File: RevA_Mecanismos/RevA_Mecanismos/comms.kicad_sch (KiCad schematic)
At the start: 12 parts, among them IC1 MAX33040EAKA+T, J2 Conn_01x03_Pin, J3 430450224, J4 430450224, J6 430450224, J7 430450224

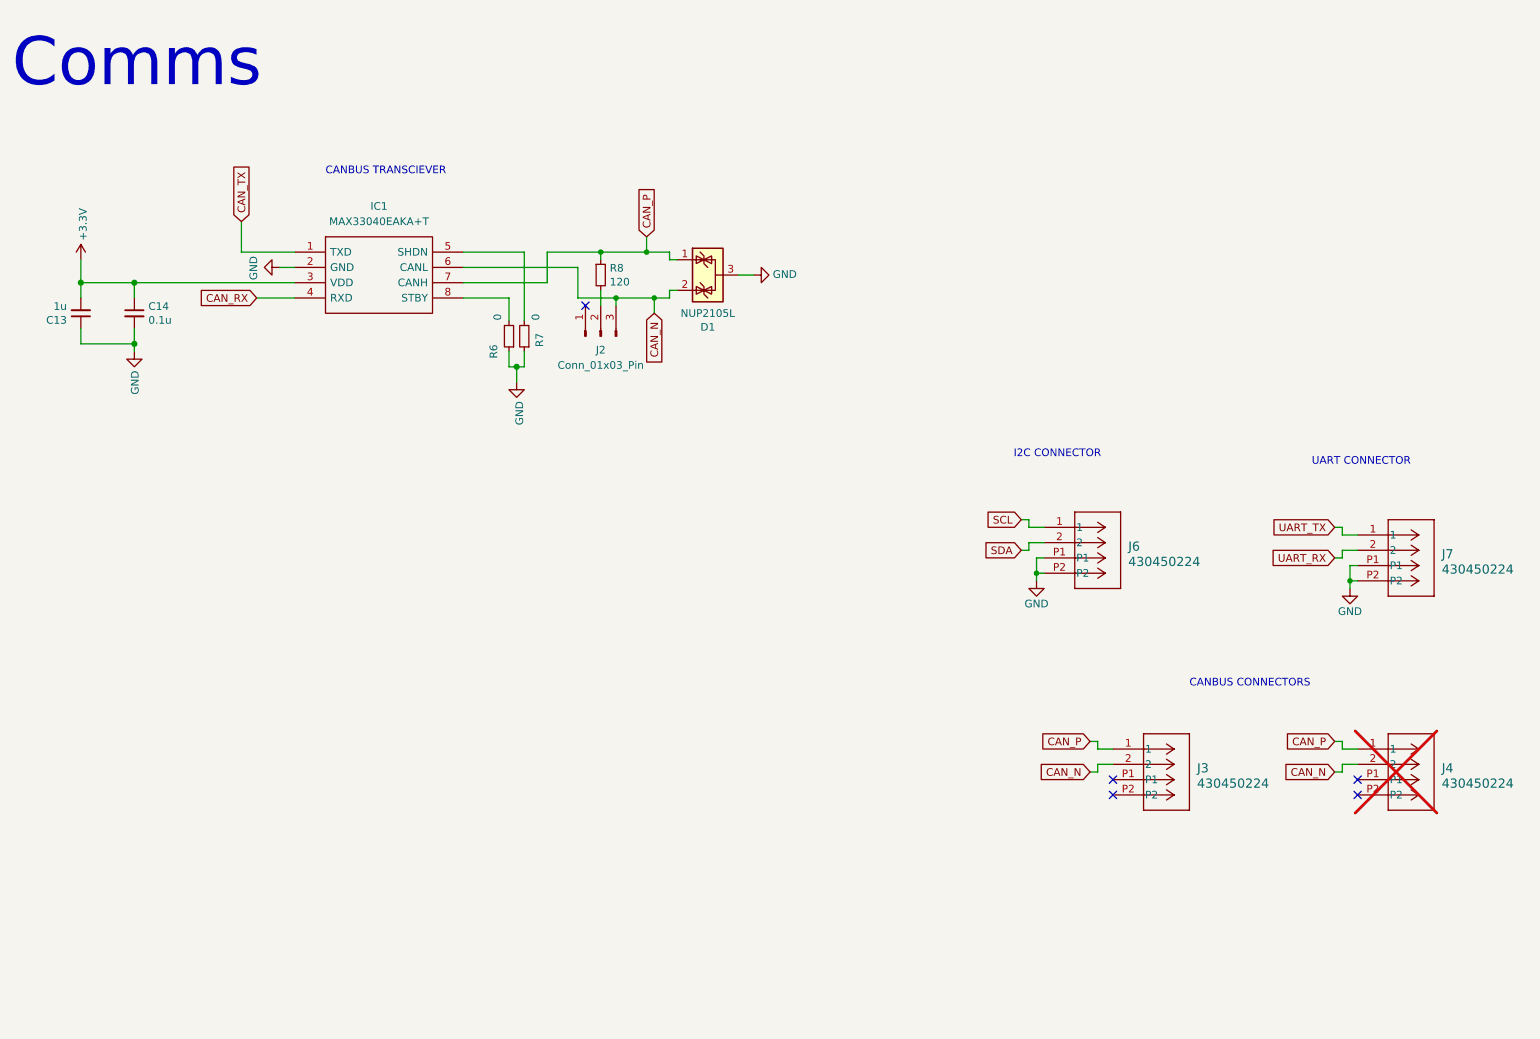
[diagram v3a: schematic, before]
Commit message: Updated STM32 USV Mechanism PCB
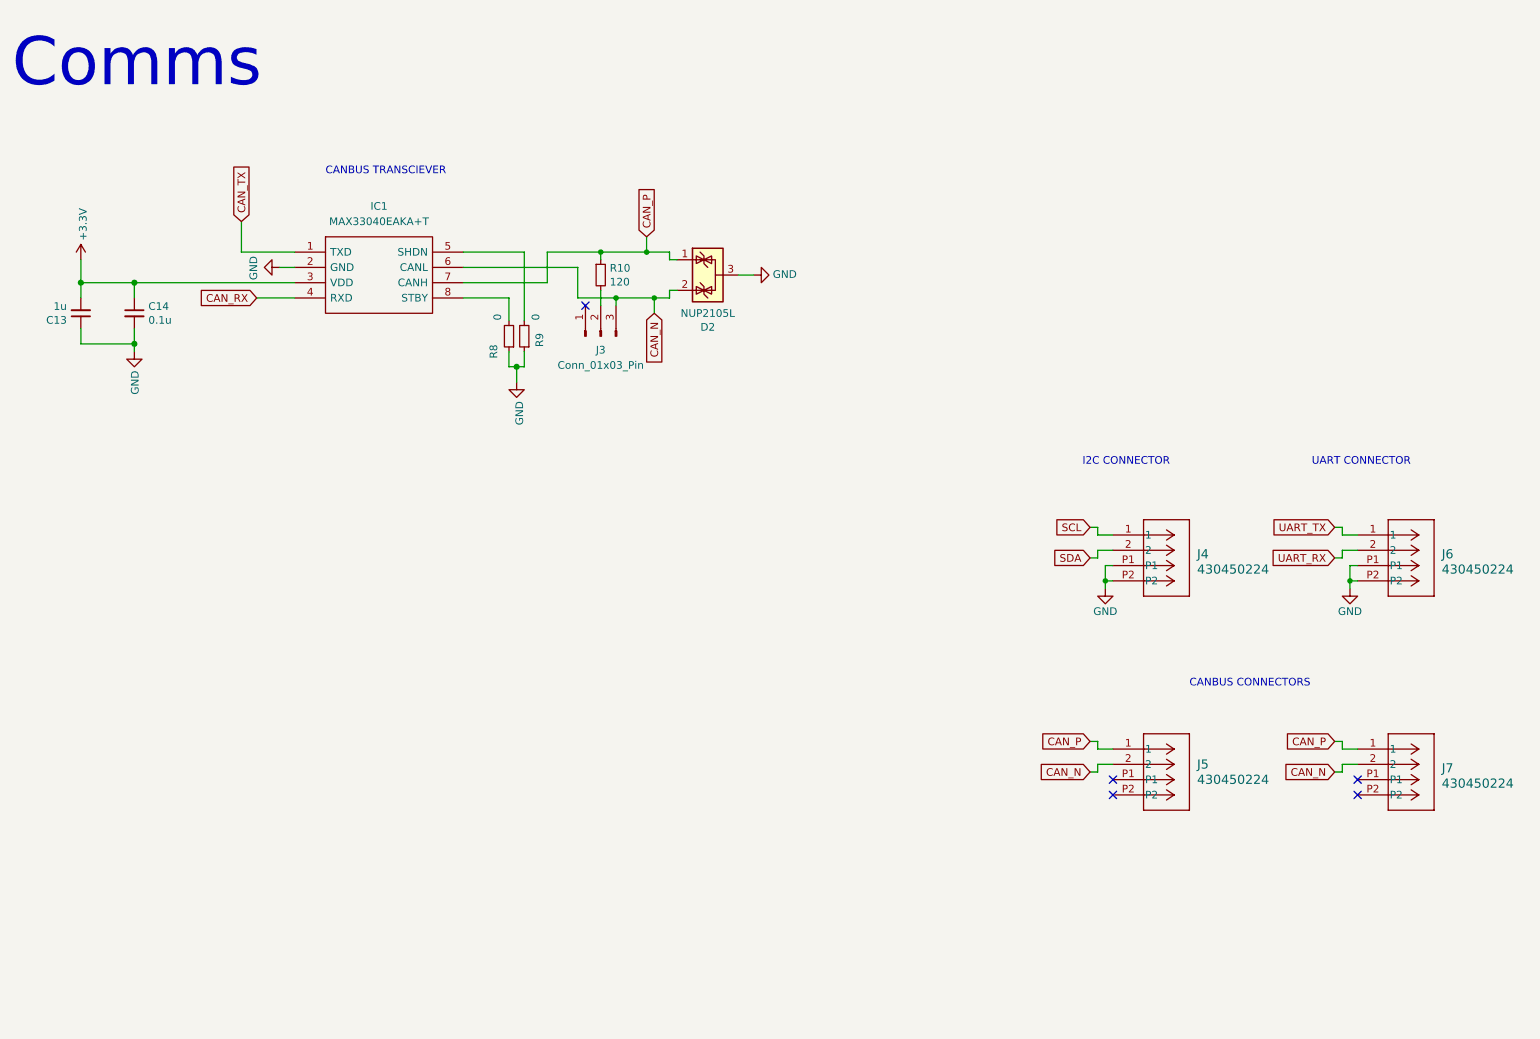
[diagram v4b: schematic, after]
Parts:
- J7: renamed from J4; now fitted
- renumbered D1 to D2, J2 to J3, J6 to J4, J3 to J5, J7 to J6, R8 to R10, R6 to R8, R7 to R9
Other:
- moved on the sheet: J4

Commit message: Complete schematic and pcb designs, routes missing and not yet complete
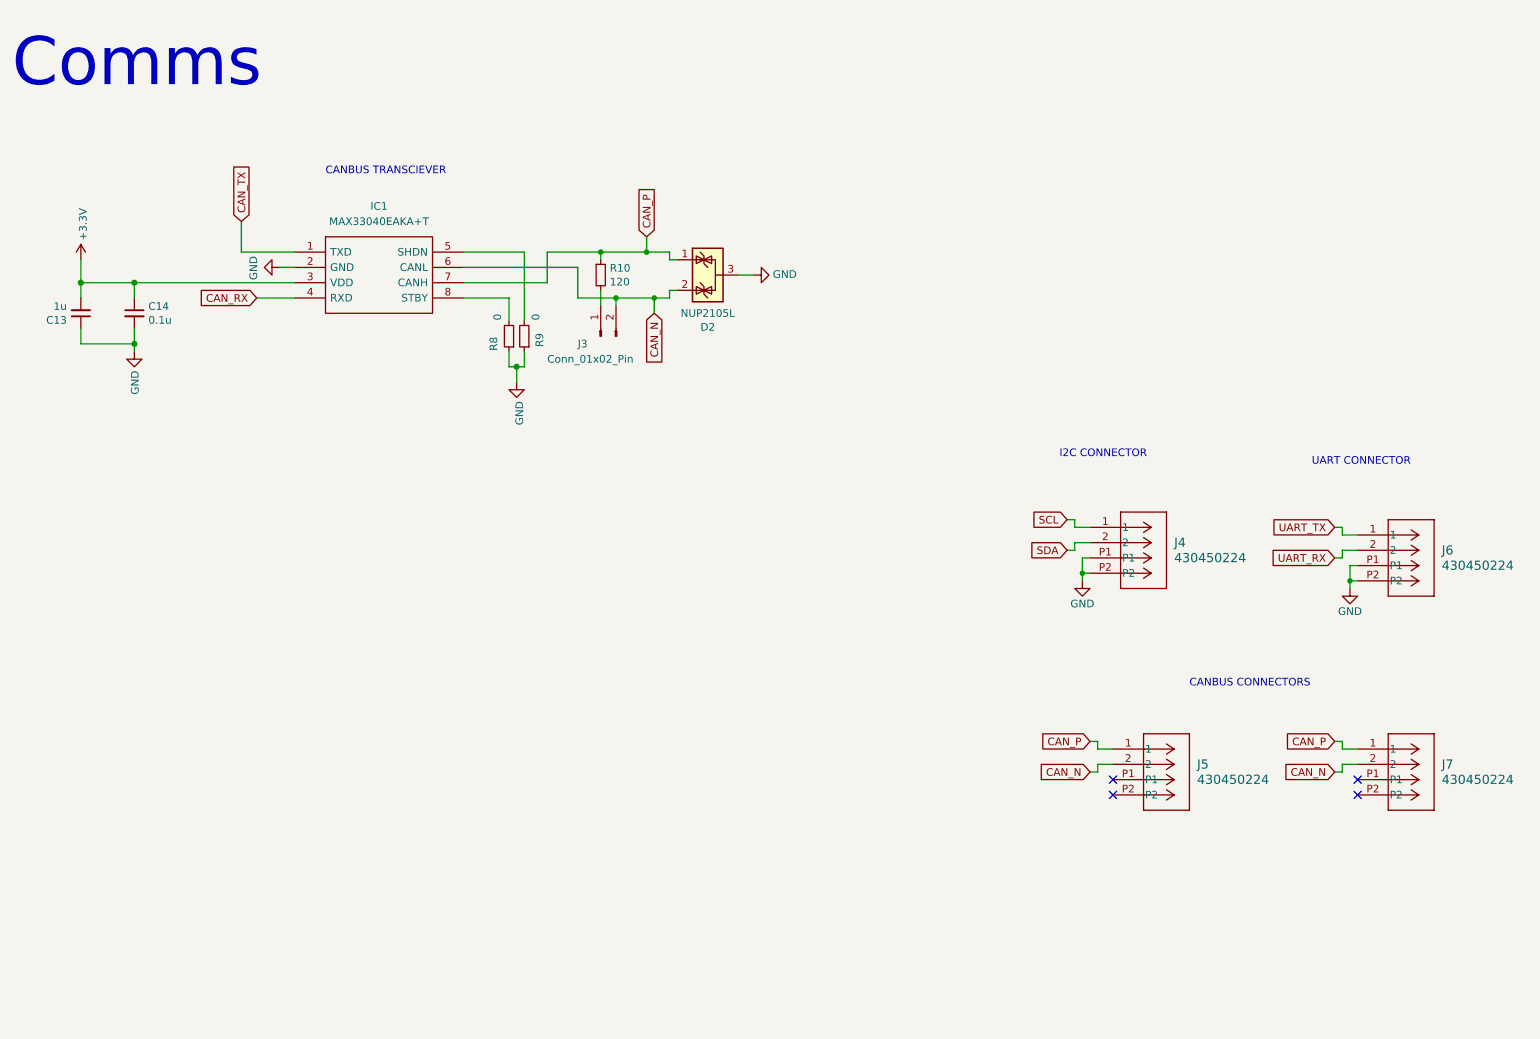
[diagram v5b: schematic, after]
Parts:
- removed J3: Conn_01x03_Pin, Connector_PinHeader_1.27mm:PinHeader_1x03_P1.27mm_Vertical, symbol Connector:Conn_01x03_Pin
- added J3: Conn_01x02_Pin, Connector_PinHeader_1.27mm:PinHeader_1x03_P1.27mm_Vertical, symbol Connector:Conn_01x02_Pin
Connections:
- net CAN_N: now also J3.2 (Pin_2)
- net at R10.2: now also J3.1 (Pin_1)
- no-connect marks 5 -> 4
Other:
- moved on the sheet: J4
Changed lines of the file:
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@@
   (junction (at 106.68 78.74) (diameter 1.016) (color 0 0 0 0)
   )
-  (junction (at 204.47 114.3) (diameter 0) (color 0 0 0 0)
+  (junction (at 200.66 113.03) (diameter 0) (color 0 0 0 0)
   )
   (junction (at 129.54 67.31) (diameter 0) (color 0 0 0 0)
@@
   (no_connect (at 246.38 147.32))
   (no_connect (at 205.74 149.86))
-  (no_connect (at 118.11 68.58))
   (wire (pts (xy 97.79 59.69) (xy 107.95 59.69))
     (stroke (width 0) (type default))
@@
     (stroke (width 0) (type solid))
   )
-  (wire (pts (xy 203.2 110.49) (xy 201.93 110.49))
+  (wire (pts (xy 199.39 109.22) (xy 198.12 109.22))
     (stroke (width 0) (type default))
   )
@@
     (stroke (width 0) (type solid))
   )
-  (wire (pts (xy 203.2 106.68) (xy 205.74 106.68))
-    (stroke (width 0) (type default))
-  )
-  (wire (pts (xy 204.47 115.57) (xy 204.47 114.3))
+  (wire (pts (xy 199.39 105.41) (xy 201.93 105.41))
+    (stroke (width 0) (type default))
+  )
+  (wire (pts (xy 200.66 114.3) (xy 200.66 113.03))
     (stroke (width 0) (type default))
   )
@@
     (stroke (width 0) (type default))
   )
-  (wire (pts (xy 203.2 110.49) (xy 203.2 109.22))
+  (wire (pts (xy 199.39 109.22) (xy 199.39 107.95))
     (stroke (width 0) (type default))
   )
@@
     (stroke (width 0) (type default))
   )
-  (wire (pts (xy 203.2 105.41) (xy 203.2 106.68))
+  (wire (pts (xy 199.39 104.14) (xy 199.39 105.41))
     (stroke (width 0) (type default))
   )
@@
     (stroke (width 0) (type solid))
   )
-  (wire (pts (xy 204.47 111.76) (xy 205.74 111.76))
-    (stroke (width 0) (type default))
-  )
-  (wire (pts (xy 204.47 114.3) (xy 204.47 111.76))
+  (wire (pts (xy 200.66 110.49) (xy 201.93 110.49))
+    (stroke (width 0) (type default))
+  )
+  (wire (pts (xy 200.66 113.03) (xy 200.66 110.49))
     (stroke (width 0) (type default))
   )
@@
     (stroke (width 0) (type default))
   )
-  (wire (pts (xy 203.2 109.22) (xy 205.74 109.22))
+  (wire (pts (xy 199.39 107.95) (xy 201.93 107.95))
     (stroke (width 0) (type default))
   )
@@
     (stroke (width 0) (type solid))
   )
-  (wire (pts (xy 201.93 105.41) (xy 203.2 105.41))
+  (wire (pts (xy 198.12 104.14) (xy 199.39 104.14))
     (stroke (width 0) (type default))
   )
@@
     (stroke (width 0) (type default))
   )
-  (wire (pts (xy 204.47 114.3) (xy 205.74 114.3))
+  (wire (pts (xy 200.66 113.03) (xy 201.93 113.03))
     (stroke (width 0) (type default))
   )
@@
     (effects (font (size 1.27 1.27)) (justify left bottom))
   )
-  (text "I2C CONNECTOR" (at 200.66 95.25 0)
+  (text "I2C CONNECTOR" (at 196.85 93.98 0)
     (effects (font (size 1.27 1.27)) (justify left bottom))
   )
@@
     )
   )
-  (global_label "SCL" (shape input) (at 201.93 105.41 180) (fields_autoplaced)
+  (global_label "SCL" (shape input) (at 198.12 104.14 180) (fields_autoplaced)
     (effects (font (size 1.27 1.27)) (justify right))
-    (property "Intersheetrefs" "${INTERSHEET_REFS}" (at 195.5166 105.41 0)
+    (property "Intersheetrefs" "${INTERSHEET_REFS}" (at 191.7066 104.14 0)
       (effects (font (size 1.27 1.27)) (justify right) hide)
     )
@@
     )
   )
-  (global_label "SDA" (shape input) (at 201.93 110.49 180) (fields_autoplaced)
+  (global_label "SDA" (shape input) (at 198.12 109.22 180) (fields_autoplaced)
     (effects (font (size 1.27 1.27)) (justify right))
-    (property "Intersheetrefs" "${INTERSHEET_REFS}" (at 195.4561 110.49 0)
+    (property "Intersheetrefs" "${INTERSHEET_REFS}" (at 191.6461 109.22 0)
       (effects (font (size 1.27 1.27)) (justify right) hide)
     )
@@
   (symbol (lib_id "Device:R_Small") (at 105.41 73.66 180) (unit 1)
     (in_bom yes) (on_board yes) (dnp no)
-    (property "Reference" "R8" (at 102.87 76.2 90)
+    (property "Reference" "R8" (at 102.87 74.93 90)
       (effects (font (size 1.27 1.27)))
     )
@@
     )
   )
-  (symbol (lib_id "power:GND") (at 204.47 115.57 0) (unit 1)
-    (in_bom yes) (on_board yes) (dnp no)
-    (property "Reference" "#PWR026" (at 204.47 121.92 0)
-      (effects (font (size 1.27 1.27)) hide)
-    )
-    (property "Value" "GND" (at 204.47 119.38 0)
+  (symbol (lib_id "power:GND") (at 200.66 114.3 0) (unit 1)
+    (in_bom yes) (on_board yes) (dnp no)
+    (property "Reference" "#PWR026" (at 200.66 120.65 0)
+      (effects (font (size 1.27 1.27)) hide)
+    )
+    (property "Value" "GND" (at 200.66 118.11 0)
       (effects (font (size 1.27 1.27)))
     )
-    (property "Footprint" "" (at 204.47 115.57 0)
-      (effects (font (size 1.27 1.27)) hide)
-    )
-    (property "Datasheet" "" (at 204.47 115.57 0)
+    (property "Footprint" "" (at 200.66 114.3 0)
+      (effects (font (size 1.27 1.27)) hide)
+    )
+    (property "Datasheet" "" (at 200.66 114.3 0)
       (effects (font (size 1.27 1.27)) hide)
     )
@@
   (symbol (lib_id "MolexConnectors:430450224") (at 246.38 106.68 0) (unit 1)
     (in_bom yes) (on_board yes) (dnp no) (fields_autoplaced)
-    (property "Reference" "J6" (at 260.35 109.855 0)
+    (property "Reference" "J6" (at 260.35 109.22 0)
       (effects (font (size 1.524 1.524)) (justify left))
     )
-    (property "Value" "430450224" (at 260.35 112.395 0)
+    (property "Value" "430450224" (at 260.35 111.76 0)
       (effects (font (size 1.524 1.524)) (justify left))
     )
@@
     )
   )
-  (symbol (lib_id "MolexConnectors:430450224") (at 205.74 106.68 0) (unit 1)
+  (symbol (lib_id "MolexConnectors:430450224") (at 201.93 105.41 0) (unit 1)
     (in_bom yes) (on_board yes) (dnp no) (fields_autoplaced)
-    (property "Reference" "J4" (at 219.71 109.855 0)
+    (property "Reference" "J4" (at 215.9 107.95 0)
       (effects (font (size 1.524 1.524)) (justify left))
     )
-    (property "Value" "430450224" (at 219.71 112.395 0)
+    (property "Value" "430450224" (at 215.9 110.49 0)
       (effects (font (size 1.524 1.524)) (justify left))
     )
-    (property "Footprint" "MolexConnectors:CON_430450224_MOL" (at 205.74 106.68 0)
+    (property "Footprint" "MolexConnectors:CON_430450224_MOL" (at 201.93 105.41 0)
       (effects (font (size 1.27 1.27) italic) hide)
     )
-    (property "Datasheet" "430450224" (at 205.74 106.68 0)
+    (property "Datasheet" "430450224" (at 201.93 105.41 0)
       (effects (font (size 1.27 1.27) italic) hide)
     )
@@
     )
   )
+  (symbol (lib_id "Connector:Conn_01x02_Pin") (at 120.65 73.66 90) (unit 1)
+    (in_bom yes) (on_board yes) (dnp no)
+    (property "Reference" "J3" (at 116.84 74.93 90)
+      (effects (font (size 1.27 1.27)) (justify right))
+    )
+    (property "Value" "Conn_01x02_Pin" (at 111.76 77.47 90)
+      (effects (font (size 1.27 1.27)) (justify right))
+    )
+    (property "Footprint" "Connector_PinHeader_1.27mm:PinHeader_1x03_P1.27mm_Vertical" (at 120.65 73.66 0)
+      (effects (font (size 1.27 1.27)) hide)
+    )
+    (property "Datasheet" "~" (at 120.65 73.66 0)
+      (effects (font (size 1.27 1.27)) hide)
+    )
+    (pin "1")
+    (pin "2")
+    (instances
+      (project "RevA_Mecanismos"
+        (path "/3a16a434-10b7-49a8-988b-273362cb395e/bcc025d3-9101-4be1-9a90-c8c5267d3d07"
+          (reference "J3") (unit 1)
+        )
+      )
+    )
+  )
   (symbol (lib_id "power:GND") (at 43.18 76.2 0) (unit 1)
     (in_bom yes) (on_board yes) (dnp no)
@@
   (symbol (lib_id "MolexConnectors:430450224") (at 246.38 142.24 0) (unit 1)
     (in_bom yes) (on_board yes) (dnp no) (fields_autoplaced)
-    (property "Reference" "J7" (at 260.35 145.415 0)
+    (property "Reference" "J7" (at 260.35 144.78 0)
       (effects (font (size 1.524 1.524)) (justify left))
     )
-    (property "Value" "430450224" (at 260.35 147.955 0)
+    (property "Value" "430450224" (at 260.35 147.32 0)
       (effects (font (size 1.524 1.524)) (justify left))
     )
@@
         )
       )
-    )
-  )
-  (symbol (lib_id "Connector:Conn_01x03_Pin") (at 120.65 73.66 90) (unit 1)
-    (in_bom yes) (on_board yes) (dnp no) (fields_autoplaced)
-    (property "Reference" "J3" (at 120.65 75.946 90)
-      (effects (font (size 1.27 1.27)))
-    )
-    (property "Value" "Conn_01x03_Pin" (at 120.65 78.486 90)
-      (effects (font (size 1.27 1.27)))
-    )
-    (property "Footprint" "Connector_PinHeader_1.27mm:PinHeader_1x03_P1.27mm_Vertical" (at 120.65 73.66 0)
-      (effects (font (size 1.27 1.27)) hide)
-    )
-    (property "Datasheet" "~" (at 120.65 73.66 0)
-      (effects (font (size 1.27 1.27)) hide)
-    )
-    (property "LCSC" "C24980" (at 120.65 73.66 0)
-      (effects (font (size 1.27 1.27)) hide)
-    )
-    (pin "1")
-    (pin "2")
-    (pin "3")
-    (instances
-      (project "RevA_Mecanismos"
-        (path "/3a16a434-10b7-49a8-988b-273362cb395e/bcc025d3-9101-4be1-9a90-c8c5267d3d07"
-          (reference "J3") (unit 1)
-        )
-      )
-      (project "stepper_module_v2"
-        (path "/60aa52ba-7ce7-4ce8-b294-2b47b8740a05/b2f014f9-4692-4aa0-971a-95a6b54039f1"
-          (reference "J?") (unit 1)
-        )
-      )
-      (project "IO_module"
-        (path "/6afa037b-8727-4bf3-bca2-b74b900c310e/f7717af0-8d00-4e6e-af2c-9831ea7ac606"
-          (reference "J?") (unit 1)
-        )
-      )
-      (project "general_module"
-        (path "/dca60769-f0dc-421e-8977-c562ab033f2a/600a6ed2-7b62-4790-b557-f682cf4705dc"
-          (reference "J?") (unit 1)
-        )
-      )

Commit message: Correction made to footprint for J3 pin header
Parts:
- J3: footprint Connector_PinHeader_1.27mm:PinHeader_1x03_P1.27mm_Vertical -> Connector_PinHeader_1.27mm:PinHeader_1x02_P1.27mm_Vertical
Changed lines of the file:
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@@
       (effects (font (size 1.27 1.27)) (justify right))
     )
-    (property "Footprint" "Connector_PinHeader_1.27mm:PinHeader_1x03_P1.27mm_Vertical" (at 120.65 73.66 0)
+    (property "Footprint" "Connector_PinHeader_1.27mm:PinHeader_1x02_P1.27mm_Vertical" (at 120.65 73.66 0)
       (effects (font (size 1.27 1.27)) hide)
     )
